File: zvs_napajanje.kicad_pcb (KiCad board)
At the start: 2 copper layers, 17 parts, among them J1 ulaz, J2 Conn_01x03_Female, Q1 IRF540N, Q2 IRF540N

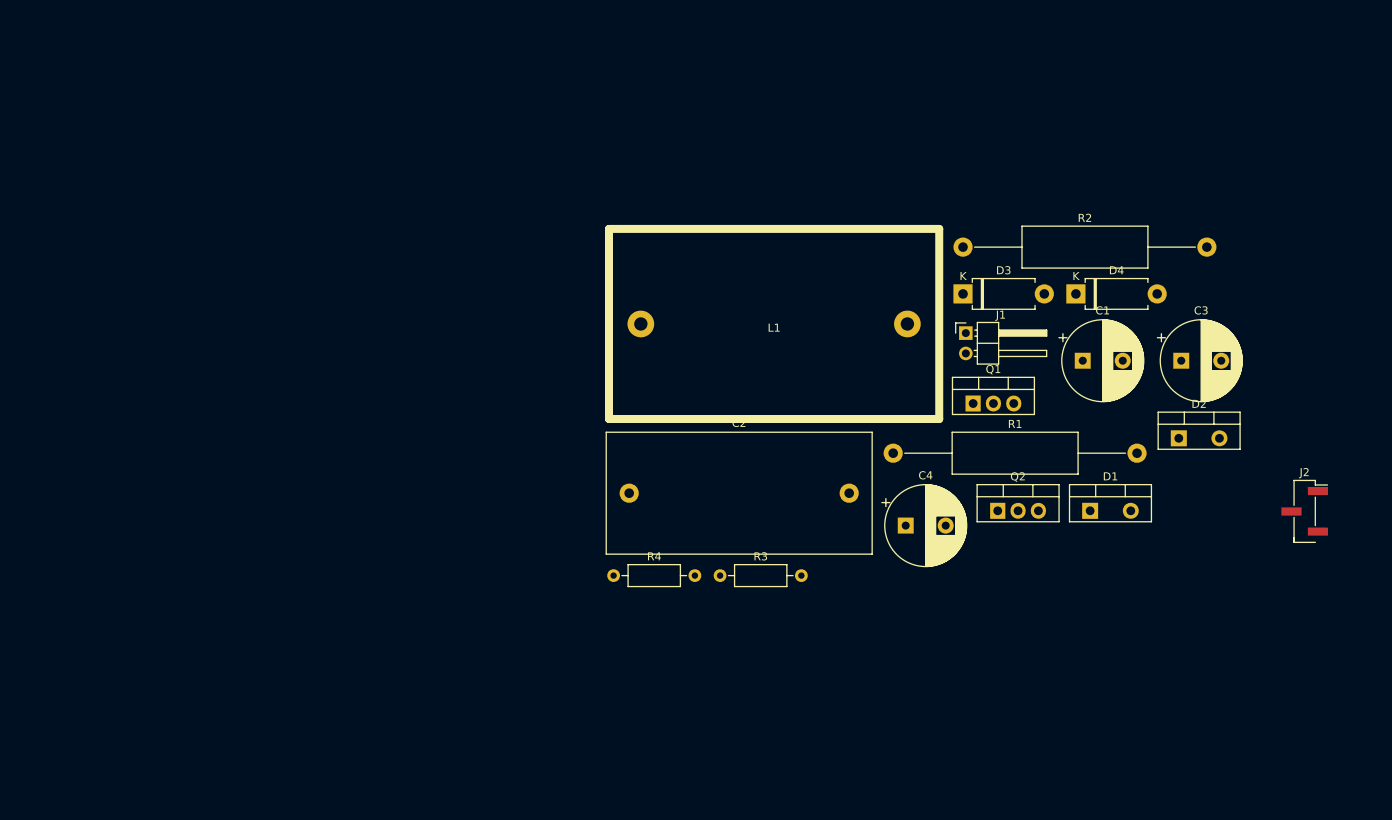
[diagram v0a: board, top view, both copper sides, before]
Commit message: Added heatsink, fixed footprints; Experimental layout
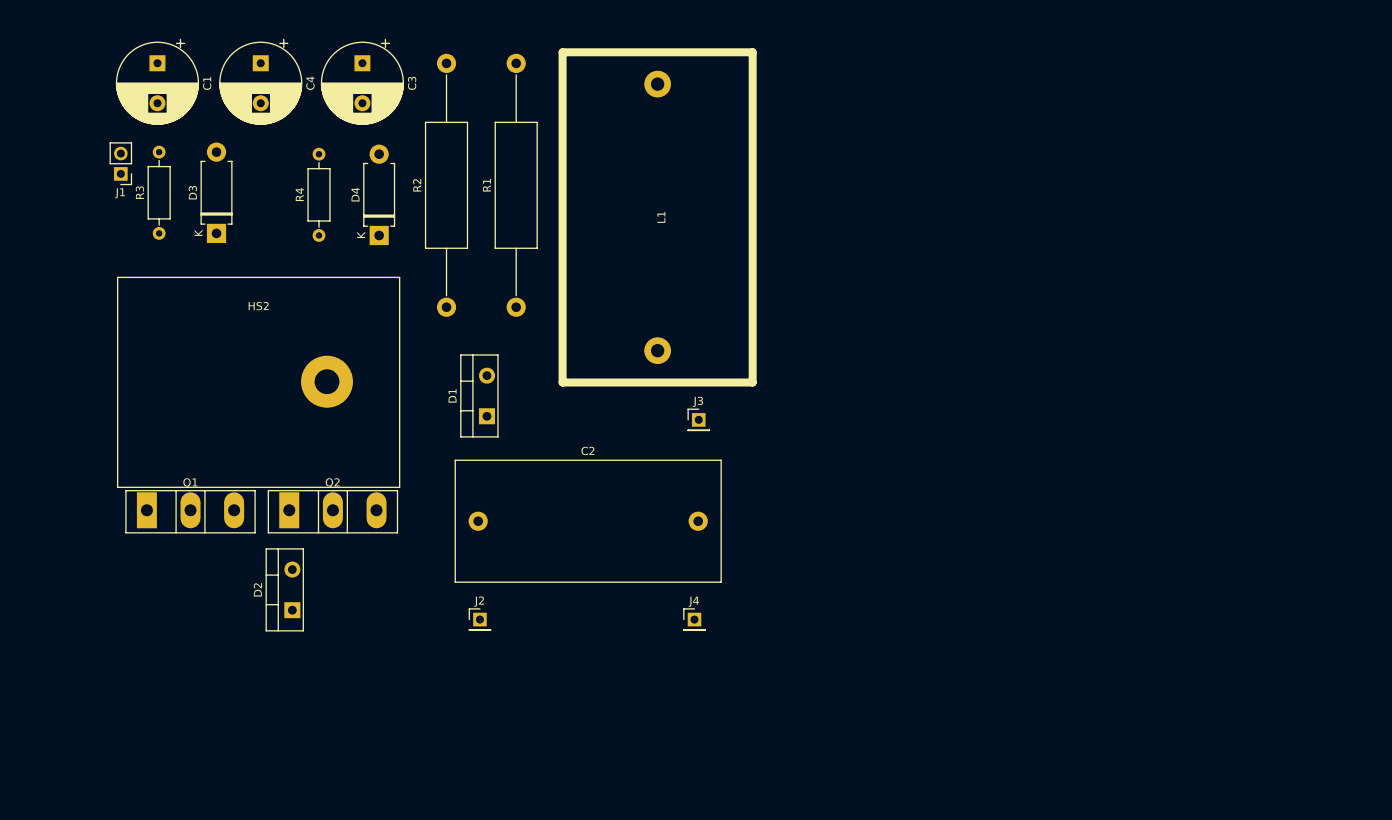
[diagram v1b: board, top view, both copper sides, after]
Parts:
- added HS2: Heatsink, Heatsink:Heatsink_35x26mm_1xFixation3mm_Fischer-SK486-35, F.Cu at (69.4, 104.7)
- added J3: Conn_01x01_Female, Connector_PinHeader_2.54mm:PinHeader_1x01_P2.54mm_Vertical, F.Cu at (115.9, 109.5)
- added J4: Conn_01x01_Female, Connector_PinHeader_2.54mm:PinHeader_1x01_P2.54mm_Vertical, F.Cu at (115.3, 134.4)
- J1: footprint Connector_PinHeader_2.54mm:PinHeader_1x02_P2.54mm_Horizontal -> Connector_PinHeader_2.54mm:PinHeader_1x02_P2.54mm_Vertical
- J2: value Conn_01x03_Female -> Conn_01x01_Female; footprint Connector_PinHeader_2.54mm:PinHeader_1x03_P2.54mm_Vertical_SMD_Pin1Right -> Connector_PinHeader_2.54mm:PinHeader_1x01_P2.54mm_Vertical
- Q1, Q2: value IRF540N -> IRFP250; footprint Package_TO_SOT_THT:TO-220-3_Vertical -> Package_TO_SOT_THT:TO-247-3_Vertical
- moved C1 121.5 mm to (48.2, 64.9), turned to 270 degrees
- moved D2 112.9 mm to (65.1, 133.2), turned to 90 degrees
- moved C3 108.9 mm to (73.8, 64.9), turned to 270 degrees
- moved J1 107.5 mm to (43.6, 78.7), turned to 180 degrees
- moved Q1 104.1 mm to (46.9, 120.8)
- moved J2 104.0 mm to (88.5, 134.4)
- moved C4 99.2 mm to (61.1, 64.9), turned to 270 degrees
- moved D3 93.6 mm to (55.6, 86.2), turned to 90 degrees
- moved Q2 88.6 mm to (64.7, 120.8)
- moved D4 87.4 mm to (75.9, 86.4), turned to 90 degrees
- moved R3 82.1 mm to (48.4, 86.2), turned to 90 degrees
- moved D1 76.3 mm to (89.4, 109.0), turned to 90 degrees
- moved R2 65.0 mm to (84.3, 95.4), turned to 90 degrees
- moved R4 56.2 mm to (68.4, 86.4), turned to 90 degrees
- moved R1 50.5 mm to (93.0, 95.4), turned to 90 degrees
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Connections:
- L1 pad 2: Net-(J2-Pad2) -> Net-(J3-Pad1)

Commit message: almost over
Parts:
- removed HS2: Heatsink, Heatsink:Heatsink_35x26mm_1xFixation3mm_Fischer-SK486-35
- added G***: LOGO, ZVSsupply:ICM_logo, F.Cu at (95.5, 71.0)
- moved J3 85.0 mm to (34.0, 86.5)
- moved R4 71.7 mm to (44.5, 154.0)
- moved D4 71.5 mm to (52.5, 154.0)
- moved J4 55.2 mm to (62.0, 148.5)
- moved L1 50.3 mm to (60.5, 86.0), turned to 0 degrees
- moved R1 45.0 mm to (70.0, 134.0)
- moved Q2 44.5 mm to (35.0, 153.9), turned to 90 degrees
- moved D1 39.7 mm to (58.5, 134.0), turned to 180 degrees
- moved R2 38.9 mm to (79.5, 134.0)
- moved R3 37.6 mm to (44.5, 123.5)
- moved D3 37.5 mm to (52.5, 123.5)
- moved J2 30.7 mm to (62.0, 119.0)
- moved D2 17.8 mm to (77.5, 146.0), turned to 180 degrees
- moved J1 14.8 mm to (34.5, 67.0)
- moved Q1 12.3 mm to (35.0, 124.0), turned to 90 degrees
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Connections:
- Q2 pad 2: VEE -> Net-(C2-Pad2)
- Q2 pad 3: Net-(C2-Pad2) -> VEE
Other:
- board outline added: 75.5 x 98.5 mm
- board text added: "ZVS high voltage supply August, 2019 by Istraživački Centar Mladih"

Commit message: almost almost over
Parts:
- moved J1 158.0 mm to (192.5, 63.5), turned to 90 degrees
- moved C1 150.8 mm to (196.1, 74.7), turned to 180 degrees
- moved J3 141.0 mm to (173.0, 63.0), turned to 270 degrees
- moved C4 139.6 mm to (196.1, 87.6), turned to 180 degrees
- moved C3 130.2 mm to (196.1, 100.3), turned to 180 degrees
- moved Q1 117.0 mm to (135.5, 64.0), turned to 0 degrees
- moved Q2 114.3 mm to (105.5, 64.0), turned to 0 degrees
- moved L1 113.1 mm to (173.5, 89.5), turned to 270 degrees
- moved G*** 107.3 mm to (188.5, 124.5), turned to 0 degrees
- moved R3 104.3 mm to (136.0, 73.5), turned to 0 degrees
- moved R4 101.0 mm to (105.5, 73.5), turned to 0 degrees
- moved D3 93.5 mm to (136.0, 81.5), turned to 0 degrees
- moved D4 89.8 mm to (105.5, 81.5), turned to 0 degrees
- moved J2 83.3 mm to (140.5, 91.0), turned to 270 degrees
- moved D1 81.6 mm to (125.5, 87.5), turned to 90 degrees
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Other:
- board size 75.5 x 98.5 mm -> 98.5 x 75.5 mm

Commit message: finished layout
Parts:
- added J5: VEE_JUMPER, Connector_PinHeader_2.54mm:PinHeader_1x01_P2.54mm_Vertical, F.Cu at (156.2, 64.0)
- added J6: VEE_JUMPER, Connector_PinHeader_2.54mm:PinHeader_1x01_P2.54mm_Vertical, F.Cu at (125.8, 64.0)
- J1: footprint Connector_PinHeader_2.54mm:PinHeader_1x02_P2.54mm_Vertical -> Connector_Wire:SolderWirePad_1x02_P5.08mm_Drill1.5mm
- moved D2 5.62 mm to (108.2, 108.5), turned to 0 degrees
- moved J1 1.80 mm to (191.0, 64.5), turned to 0 degrees
- moved J3 0.71 mm to (173.5, 63.5)
- moved J2 0.50 mm to (141.0, 91.0)
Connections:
- D4 pad 2: VEE -> Net-(D4-Pad2)
- Q2 pad 3: VEE -> Net-(D4-Pad2)
- R4 pad 2: VEE -> Net-(D4-Pad2)
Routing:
- net Net-(C2-Pad1): track 0.00 -> 120.1 mm
- net VEE: track 0.00 -> 111.1 mm
- net Net-(C2-Pad2): track 0.00 -> 106.2 mm
- net VDD: track 0.00 -> 90.6 mm
- net Net-(D2-Pad2): track 0.00 -> 62.1 mm
- net Net-(D1-Pad2): track 0.00 -> 50.4 mm
- net Net-(D4-Pad2): track 0.00 -> 27.1 mm
- net Net-(J3-Pad1): track 0.00 -> 9.34 mm
